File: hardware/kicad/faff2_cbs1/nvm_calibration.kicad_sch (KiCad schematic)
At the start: 15 parts, among them U801 24FC16T-I/OT

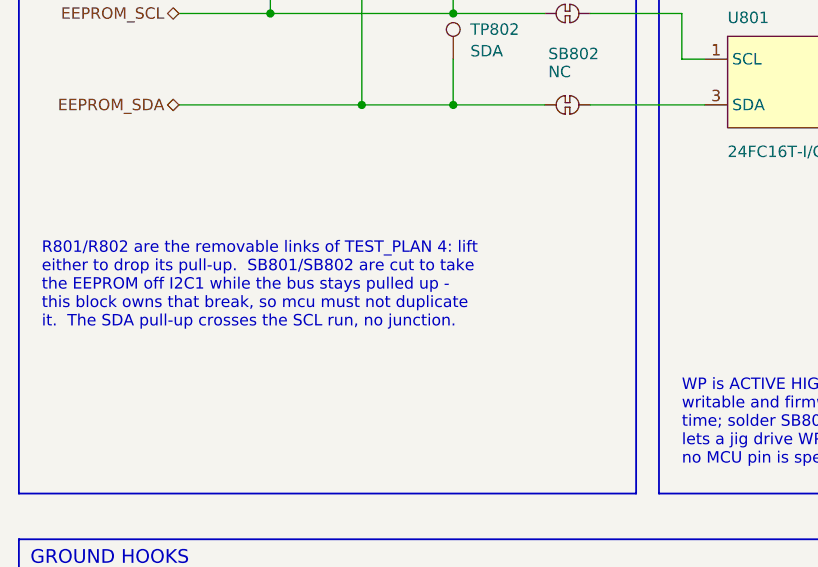
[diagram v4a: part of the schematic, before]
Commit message: review r3 item 4: respace every grazing placement, and rehome the TIM1 note
Round 2 left thirteen power-symbol names grazing something and pinned the
labels. Item 1's checker turned thirteen into sixty once labels and bodies
became subjects and the font model learned that block titles are bold 1.778 -
40% wider per character than the 1.27 it had assumed, which is how a 35 mm
title came back as 25. Fifty-seven are now clear. ERC 0/0 and node sets
identical: every change here is geometry.

The dominant defect, ten times over, is a power symbol's arrow with a vertex
exactly on a wire that runs past it and does not connect - the same thing the
captain screenshotted, nine more times. Each moves along its own stub: GND
arrows up, rail arrows down, because a rail arrow's name sits above it and
moving up only puts the text where the arrow was.

The rest: six bold titles wider than their block, eight notes and labels running
out through a border, twelve pinned names overlapped by a neighbour that moved
instead, and both 5 V PWR_FLAGs, which move onto the test-point stub below where
their 9.5 mm name has clear air.

Two checker corrections came out of doing the work. Fourteen findings were text
over its OWN conductor - a label on its wire with a branch of the same net
dropping through the text, which is what "the wire must extend under the entire
label" asks for; wire_nodes() groups segments into electrical nodes and excuses
the whole node. And field-against-field comparison had been lost in the
subject/obstacle rewrite - reference-against-value is the commonest defect there
is, and it went unnoticed until a render showed PWR_FLAG 0.86 mm inside a
neighbouring 100nF on a sheet the checker called clean.

The TIM1 note: round 2 recorded that nothing 47.6 x 8.7 fitted anywhere in
motor_drive block 4. With item 1's geometry that was wrong - 495 positions fit.
It now sits beside U1101's logic inputs, which is what it describes.

Three are left, both explained in the decisions file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
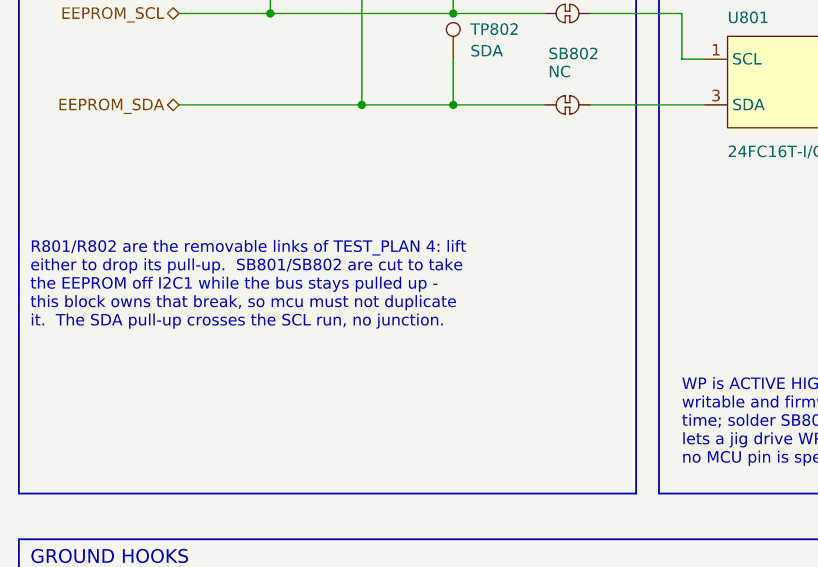
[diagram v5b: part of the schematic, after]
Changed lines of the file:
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@@
 	(text "R801/R802 are the removable links of TEST_PLAN 4: lift\neither to drop its pull-up.  SB801/SB802 are cut to take\nthe EEPROM off I2C1 while the bus stays pulled up -\nthis block owns that break, so mcu must not duplicate\nit.  The SDA pull-up crosses the SCL run, no junction."
 		(exclude_from_sim no)
-		(at 17.7800 66.0400 0)
+		(at 16.51 66.04 0)
 		(effects
 				(font
